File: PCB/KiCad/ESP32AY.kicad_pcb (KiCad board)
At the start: 2 copper layers, 55 x 100 mm, 116 parts, among them J1 USB_C_Receptacle_USB2.0_14P, J2 MiniJack, J3 SD Card, Q1 BC807, Q2 BC817, Q3 BC817, SW1 Check bat, SW2 EN, SW3 BOOT, U1 AY-3-8910, U10 DS3231MZ, U11 24LC256, U2 AY-3-8910, U3 CH340C, U4 ESP32-WROOM-32, U5 TPA6130A2RTJTG4, U6 IP5306, U7 AMS1117-3.3, U8 74HC595, U9 74HC595, Y3 12MHz

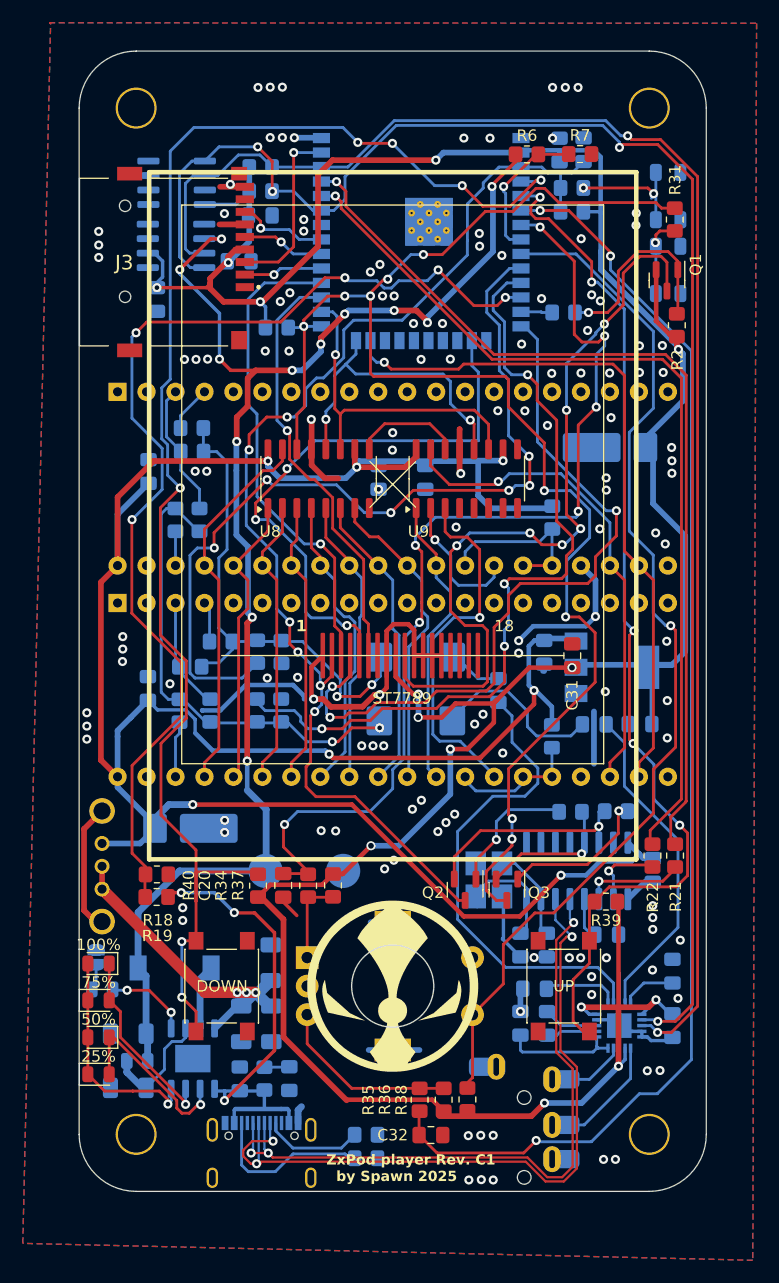
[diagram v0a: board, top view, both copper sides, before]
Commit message: Rev.C1 - initial PCM5102A DAC support
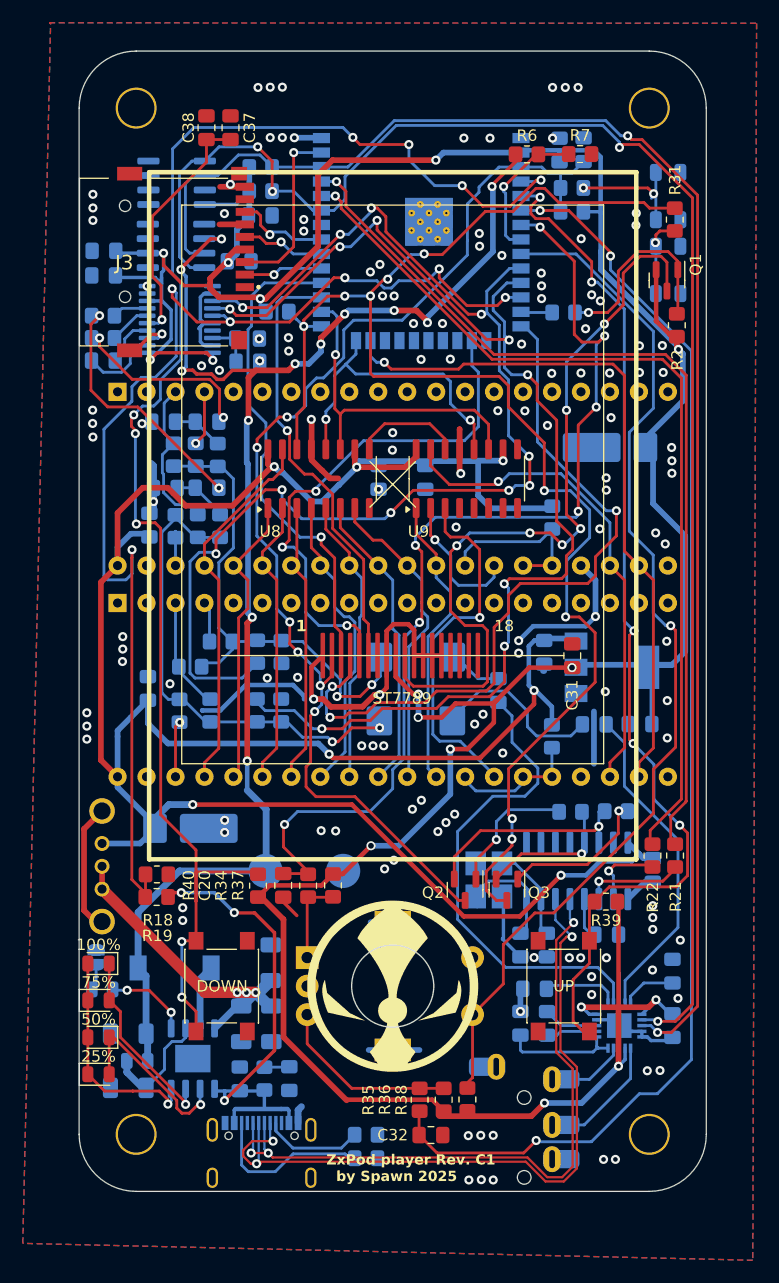
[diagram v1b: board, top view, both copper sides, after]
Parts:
- added C37: 10uf, Capacitor_SMD:C_0805_2012Metric_Pad1.18x1.45mm_HandSolder, F.Cu at (33.3, 26.7)
- added C38: 100n, Capacitor_SMD:C_0805_2012Metric_Pad1.18x1.45mm_HandSolder, F.Cu at (31.2, 26.7)
- added C39: 10uf, Capacitor_SMD:C_0805_2012Metric_Pad1.18x1.45mm_HandSolder, B.Cu at (34.8, 47.2)
- added C40: 100n, Capacitor_SMD:C_0805_2012Metric_Pad1.18x1.45mm_HandSolder, B.Cu at (34.8, 45.2)
- added C41: 2.2uf, Capacitor_SMD:C_0805_2012Metric_Pad1.18x1.45mm_HandSolder, B.Cu at (22.1, 47.1)
- added C42: 10uf, Capacitor_SMD:C_0805_2012Metric_Pad1.18x1.45mm_HandSolder, B.Cu at (31.2, 52.5)
- added C43: 10uf, Capacitor_SMD:C_0805_2012Metric_Pad1.18x1.45mm_HandSolder, B.Cu at (31.2, 58.3)
- added C44: 2.2nf, Capacitor_SMD:C_0805_2012Metric_Pad1.18x1.45mm_HandSolder, B.Cu at (27.4, 52.5)
- added C45: 2.2nf, Capacitor_SMD:C_0805_2012Metric_Pad1.18x1.45mm_HandSolder, B.Cu at (27.6, 58.3)
- added C46: 100n, Capacitor_SMD:C_0805_2012Metric_Pad1.18x1.45mm_HandSolder, B.Cu at (22.1, 39.7)
- added R43: 10K, Resistor_SMD:R_0805_2012Metric_Pad1.20x1.40mm_HandSolder, B.Cu at (22.1, 45.2)
- added R44: 10K, Resistor_SMD:R_0805_2012Metric_Pad1.20x1.40mm_HandSolder, B.Cu at (22.1, 43.2)
- added R45: 1K, Resistor_SMD:R_0805_2012Metric_Pad1.20x1.40mm_HandSolder, B.Cu at (32.4, 61.6)
- added R46: 1K, Resistor_SMD:R_0805_2012Metric_Pad1.20x1.40mm_HandSolder, B.Cu at (32.2, 55.4)
- added U12: PCM5102A, Package_SO:TSSOP-20_4.4x6.5mm_P0.65mm, B.Cu at (28.8, 43.5)
- U11: value 24LC256 -> MB85RC256V
- moved C36 6.31 mm to (22.2, 37.5), turned to 180 degrees
- moved C2 4.70 mm to (26.2, 61.6)
- moved R9 2.36 mm to (30.2, 55.4), turned to 90 degrees
- moved R10 1.64 mm to (28.3, 55.4), turned to -90 degrees
- moved R30 1.40 mm to (37.4, 42.8)
- moved R12 0.56 mm to (28.4, 61.7)
- moved R11 0.55 mm to (30.4, 61.6)
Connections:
- net DAC_SOUND_L renamed DAC_BCK
- net DAC_SOUND_R renamed DAC_DAT
- net USB_SENS renamed DAC_LRCK
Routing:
- net DAC_DAT: track 70.8 -> 105.6 mm, vias 4 -> 8
- net DAC_BCK: track 75.0 -> 107.7 mm, vias 6 -> 10
- net +3.3V: track 283.4 -> 307.1 mm, vias 14 -> 16
- net Net-(C43-Pad2): track 0.00 -> 22.3 mm, vias 0 -> 2
- net Net-(U12-VNEG): track 0.00 -> 21.8 mm, vias 0 -> 1
- net GND: track 119.5 -> 137.4 mm, vias 132 -> 138
- net Net-(C42-Pad2): track 0.00 -> 16.7 mm, vias 0 -> 2
- net DAC_LRCK: track 93.9 -> 104.9 mm, vias 5 -> 6
- net Net-(U12-CAPP): track 0.00 -> 6.96 mm
- net PCM_R: track 0.00 -> 4.85 mm
- net Net-(U12-CAPM): track 0.00 -> 4.52 mm
- net PCM_L: track 0.00 -> 4.51 mm
- net TFT_CS: track 50.6 -> 46.4 mm
- net Net-(U12-LDOO): track 0.00 -> 4.11 mm
- net Net-(U12-OUTL): track 0.00 -> 3.68 mm
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
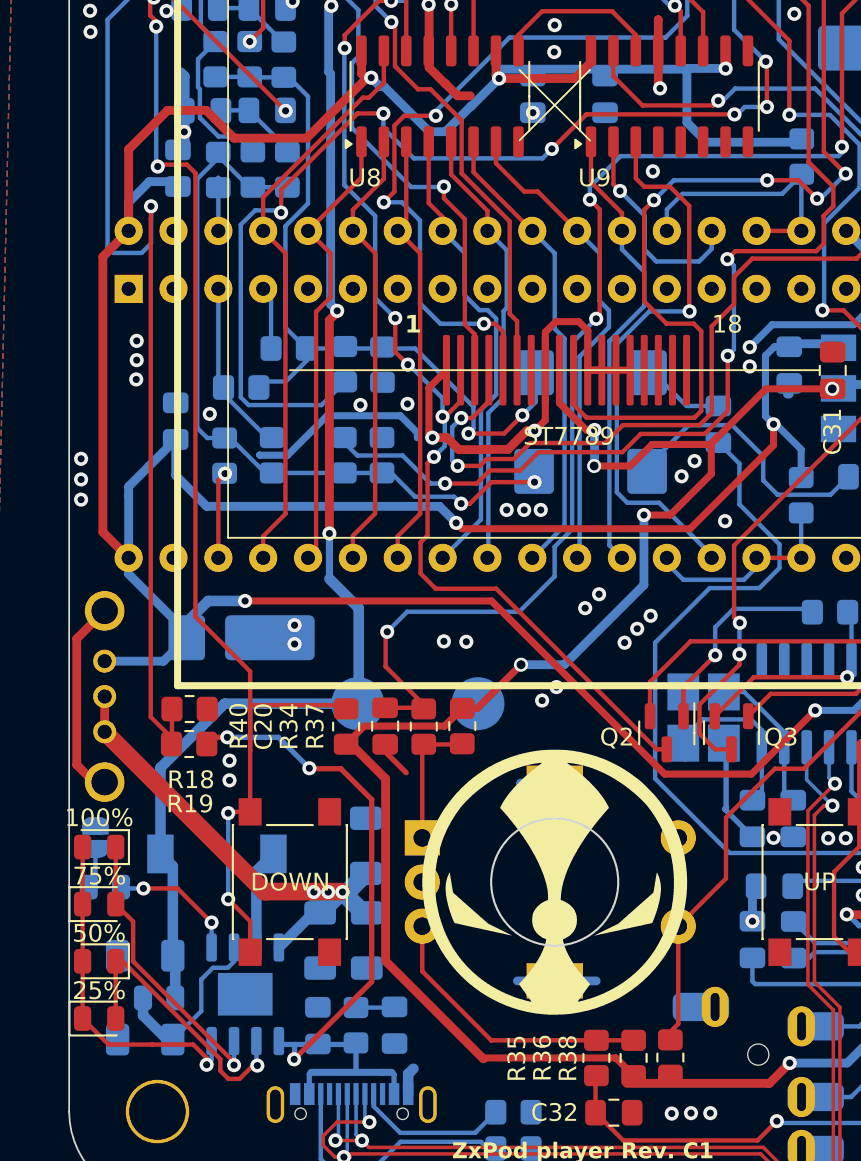
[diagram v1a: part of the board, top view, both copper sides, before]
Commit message: Updated rev.C1 - added JST-PH connector
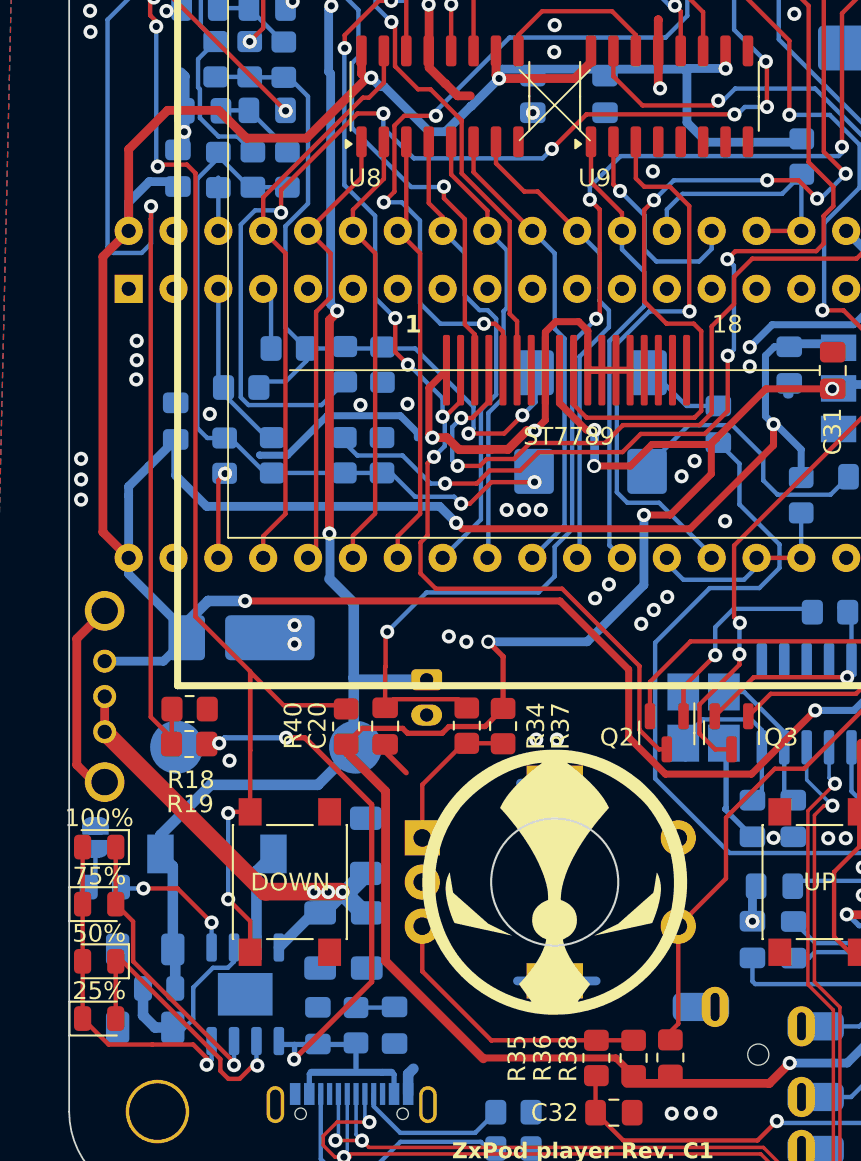
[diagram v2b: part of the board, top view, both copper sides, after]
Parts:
- added J4: Battery, Connector_JST:JST_PH_S2B-PH-K_1x02_P2.00mm_Horizontal, B.Cu at (40.2, 90.5)
- BAT+1: value BAT+ -> +
- BAT-1: value BAT- -> -
- moved BAT-1 17.2 mm to (26.1, 94.4)
- moved BAT+1 2.47 mm to (36.2, 94.4)
- moved R34 2.44 mm to (42.5, 93.1)
- moved R37 2.31 mm to (44.6, 93.2)
- moved C30 0.69 mm to (24.3, 110.2)
- moved R24 0.53 mm to (25.1, 108.0)
- moved C19 0.36 mm to (24.3, 105.8)
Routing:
- net +3.3V: track 307.1 -> 310.7 mm
- net BT_DN: track 133.1 -> 135.8 mm
- net Bat+: track 130.5 -> 133.2 mm
- net +5V: track 213.6 -> 215.8 mm
- net ESP_EN: track 103.3 -> 105.4 mm
- net ENC_A: track 88.8 -> 90.9 mm
- net Net-(Encoder1-PadA): track 7.57 -> 8.30 mm
- net GND: track 137.4 -> 137.5 mm, vias 138 -> 137
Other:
- board text added: "+"
- board text added: "Battery"
- board text removed: "LiPo Battery 2000 mAh"

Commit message: Rev.C2 initial revision
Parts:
- removed the C21 at (36.9, 105.3)
- removed the C22 at (36.8, 99.9)
- removed the C23 at (34.2, 105.3)
- removed the C30 at (24.3, 110.2)
- removed the R24 at (25.1, 108.0)
- removed the R25 at (22.0, 102.3)
- removed the SW1 at (21.5, 99.5)
- removed the U6 at (30.0, 108.4)
- added C14: 22uf, Capacitor_SMD:C_1206_3216Metric_Pad1.33x1.80mm_HandSolder, B.Cu at (26.7, 95.9)
- added C17: 22uf, Capacitor_SMD:C_1206_3216Metric_Pad1.33x1.80mm_HandSolder, B.Cu at (31.8, 92.0)
- added R10: 1k, Resistor_SMD:R_0805_2012Metric_Pad1.20x1.40mm_HandSolder, F.Cu at (26.6, 109.7)
- added R16: 2k*, Resistor_SMD:R_0805_2012Metric_Pad1.20x1.40mm_HandSolder, B.Cu at (40.6, 110.1)
- added R19: 47k, Resistor_SMD:R_0805_2012Metric_Pad1.20x1.40mm_HandSolder, F.Cu at (27.4, 98.8)
- added R20: 6.2k, Resistor_SMD:R_0805_2012Metric_Pad1.20x1.40mm_HandSolder, F.Cu at (27.4, 102.8)
- added R21: 1k, Resistor_SMD:R_0805_2012Metric_Pad1.20x1.40mm_HandSolder, F.Cu at (21.9, 103.1)
- added U4: TP4056, Package_SO:SOIC-8-1EP_3.9x4.9mm_P1.27mm_EP2.41x3.3mm_ThermalVias, B.Cu at (35.0, 103.5)
- added U7: SDB628, Package_TO_SOT_SMD:SOT-23-6_Handsoldering, B.Cu at (25.9, 101.1)
- D1: value 25% -> OK
- D2: value 50% -> CHRG
- D3: value 75% -> SS14; footprint LED_SMD:LED_0805_2012Metric -> Diode_SMD:D_SMA; moved to B.Cu
- D4: value 100% -> PWR
- L1: value 1UH -> 22uH; footprint Inductor_SMD:L_7.3x7.3_H3.5 -> Inductor_SMD:L_Bourns_SRN8040TA
- moved BAT-1 24.6 mm to (50.5, 91.8)
- moved C11 13.2 mm to (35.1, 98.1), turned to 180 degrees
- moved D3 9.80 mm to (30.6, 99.2), turned to -90 degrees
- moved BAT+1 8.85 mm to (44.7, 91.8)
- moved L1 7.38 mm to (26.1, 107.4), turned to 0 degrees
- turned D1 to 180 degrees
- renumbered C4 to C1, C18 to C10, C19 to C11, C2 to C12, C28 to C13, C36 to C15, C35 to C16, C1 to C18, C31 to C19, C3 to C2, C29 to C20, C46 to C21, C27 to C22, C41 to C23, C37 to C24, C38 to C25, C42 to C26, C44 to C27, C43 to C28, C39 to C29, C16 to C3, C45 to C30, C40 to C31, C11 to C32, C12 to C33, C13 to C34, C14 to C35, C33 to C36, C34 to C37, C10 to C38, C5 to C39, C26 to C4, C15 to C40, C9 to C41, C8 to C42, C7 to C43, C6 to C44, C24 to C5, C20 to C6, C32 to C7, C25 to C8, C17 to C9, J4 to J2, J2 to J4, R40 to R1, R38 to R11, R19 to R12, R18 to R13, R6 to R14, R7 to R15, R31 to R17, R29 to R18, R39 to R2, R20 to R22, R3 to R23, R28 to R24, R30 to R25, R43 to R26, R44 to R27, R1 to R28, R21 to R29, R41 to R3, R22 to R30, R2 to R31, R4 to R32, R5 to R33, R12 to R34, R9 to R35, R17 to R36, R14 to R37, R33 to R38, R32 to R39, R42 to R4, R11 to R40, R10 to R41, R16 to R42, R15 to R43, R26 to R44, R27 to R45, R13 to R46, R8 to R47, R45 to R48, R46 to R49, R23 to R5, R34 to R6, R35 to R7, R37 to R8, R36 to R9, S2 to S1, S4 to S2, S6 to S3, SW3 to SW1, U7 to U1, U12 to U10, U4 to U11, U3 to U12, U5 to U13, U8 to U2, U9 to U3, U1 to U5, U10 to U6, U2 to U8, U11 to U9, Y3 to Y1
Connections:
- D2 pad 1: Net-(D1-A) -> Net-(D2-K)
- D2 pad 2: Net-(D1-K) -> Net-(D1-A)
- D3 pad 1: Net-(D1-K) -> +5V
- D4 pad 1: Net-(D3-A) -> GND
- D4 pad 2: Net-(D1-K) -> Net-(D4-A)
- L1 pad 1: Net-(U6-SW) -> /STPUP_VIN
- L1 pad 2: Bat+ -> Net-(D3-A)
- S3 pad 1: Net-(U6-Vout) -> Bat+
- S3 pad 2: Net-(U6-Vout) -> Bat+
- S3 pad 3: +5V -> /STPUP_VIN
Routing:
- net Net-(U6-Vout): track 29.3 -> 0.00 mm, vias 3 -> 0
- net /STPUP_VIN: track 0.00 -> 27.2 mm
- net +5V: track 215.8 -> 232.2 mm, vias 7 -> 8
- net Net-(D2-K): track 0.00 -> 16.1 mm, vias 0 -> 1
- net Net-(U6-BAT): track 10.1 -> 0.00 mm
- net Bat+: track 133.2 -> 141.9 mm, vias 12 -> 14
- net Net-(U6-KEY): track 7.38 -> 0.00 mm, vias 2 -> 0
- net Net-(U4-PROG): track 0.00 -> 7.18 mm
- net Vin: track 43.1 -> 49.9 mm
- net Net-(D1-A): track 16.1 -> 9.73 mm, vias 1 -> 0
- net Net-(D3-A): track 16.5 -> 10.7 mm, vias 1 -> 0
- net Net-(U6-SW): track 5.70 -> 0.00 mm
- net GND: track 137.5 -> 142.8 mm, vias 137 -> 142
- net BT_DN: track 135.8 -> 131.2 mm, vias 9 -> 10
- net Net-(U7-FB): track 0.00 -> 4.27 mm, vias 0 -> 1
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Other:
- board text added: "ZxPod player Rev. C2 by Spawn 2025"
- board text removed: "ZxPod player Rev. C1 by Spawn 2025"
